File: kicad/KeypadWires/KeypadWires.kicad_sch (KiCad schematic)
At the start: 3 parts, among them J1 Cable, J2 Controller, J3 Raspberry

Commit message: Fixed keypad wiring schematics
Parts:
- removed J1: Cable, symbol Connector_Generic:Conn_02x04_Odd_Even
- added J1: Keypad, symbol Connector_Generic:Conn_02x03_Odd_Even
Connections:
- net +3.3V is gone; now on net +5V: J3.3
- net +5V: now also J1.2 (Pin_2)
- net GND: now also J1.6 (Pin_6)
- net RS232_IN: now also J1.3 (Pin_3)
- net RS232_OUT: now also J1.4 (Pin_4)
- net SCL: now also J1.5 (Pin_5)
- net SDA: now also J1.1 (Pin_1)
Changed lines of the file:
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@@
 	(wire
 		(pts
-			(xy 182.88 90.17) (xy 182.88 86.36)
+			(xy 182.88 92.71) (xy 179.07 92.71)
 		)
 		(stroke
@@
 	(wire
 		(pts
-			(xy 189.23 92.71) (xy 189.23 86.36)
-		)
-		(stroke
-			(width 0)
-			(type default)
-		)
-	)
-	(wire
-		(pts
 			(xy 180.34 97.79) (xy 180.34 99.06)
 		)
@@
 	(wire
 		(pts
-			(xy 179.07 90.17) (xy 182.88 90.17)
-		)
-		(stroke
-			(width 0)
-			(type default)
-		)
-	)
-	(wire
-		(pts
 			(xy 93.98 121.92) (xy 104.14 121.92)
 		)
@@
 	(wire
 		(pts
-			(xy 179.07 92.71) (xy 189.23 92.71)
-		)
-		(stroke
-			(width 0)
-			(type default)
-		)
-	)
-	(wire
-		(pts
 			(xy 93.98 125.73) (xy 93.98 121.92)
+		)
+		(stroke
+			(width 0)
+			(type default)
+		)
+	)
+	(wire
+		(pts
+			(xy 182.88 86.36) (xy 182.88 92.71)
 		)
 		(stroke
@@
 	)
 	(symbol
+		(lib_id "power:+5V")
+		(at 127 116.84 0)
+		(unit 1)
+		(exclude_from_sim no)
+		(in_bom yes)
+		(on_board yes)
+		(dnp no)
+		(fields_autoplaced yes)
+		(property "Reference" "#PWR01"
+			(at 127 120.65 0)
+			(effects
+				(font
+					(size 1.27 1.27)
+				)
+				(hide yes)
+			)
+		)
+		(property "Value" "+5V"
+			(at 127 111.76 0)
+			(effects
+				(font
+					(size 1.27 1.27)
+				)
+			)
+		)
+		(property "Footprint" ""
+			(at 127 116.84 0)
+			(effects
+				(font
+					(size 1.27 1.27)
+				)
+				(hide yes)
+			)
+		)
+		(property "Datasheet" ""
+			(at 127 116.84 0)
+			(effects
+				(font
+					(size 1.27 1.27)
+				)
+				(hide yes)
+			)
+		)
+		(property "Description" "Power symbol creates a global label with name \"+5V\""
+			(at 127 116.84 0)
+			(effects
+				(font
+					(size 1.27 1.27)
+				)
+				(hide yes)
+			)
+		)
+		(pin "1"
+		)
+		(instances
+			(project "KeypadWires"
+				(path "/a35776e5-918f-4787-bc96-ea4223b78852"
+					(reference "#PWR01")
+					(unit 1)
+				)
+			)
+		)
+	)
+	(symbol
 		(lib_id "power:GND")
 		(at 93.98 97.79 0)
@@
 	)
 	(symbol
-		(lib_id "Connector_Generic:Conn_02x04_Odd_Even")
-		(at 171.45 92.71 0)
-		(unit 1)
-		(exclude_from_sim no)
-		(in_bom yes)
-		(on_board yes)
-		(dnp no)
-		(fields_autoplaced yes)
-		(property "Reference" "J1"
-			(at 172.72 83.82 0)
-			(effects
-				(font
-					(size 1.27 1.27)
-				)
-			)
-		)
-		(property "Value" "Cable"
-			(at 172.72 86.36 0)
-			(effects
-				(font
-					(size 1.27 1.27)
-				)
-			)
-		)
-		(property "Footprint" ""
-			(at 171.45 92.71 0)
-			(effects
-				(font
-					(size 1.27 1.27)
-				)
-				(hide yes)
-			)
-		)
-		(property "Datasheet" "~"
-			(at 171.45 92.71 0)
-			(effects
-				(font
-					(size 1.27 1.27)
-				)
-				(hide yes)
-			)
-		)
-		(property "Description" "Generic connector, double row, 02x04, odd/even pin numbering scheme (row 1 odd numbers, row 2 even numbers), script generated (kicad-library-utils/schlib/autogen/connector/)"
-			(at 171.45 92.71 0)
-			(effects
-				(font
-					(size 1.27 1.27)
-				)
-				(hide yes)
-			)
-		)
-		(pin "8"
-		)
-		(pin "3"
-		)
-		(pin "2"
-		)
-		(pin "7"
-		)
-		(pin "6"
-		)
-		(pin "5"
-		)
-		(pin "1"
-		)
-		(pin "4"
-		)
-		(instances
-			(project "KeypadWires"
-				(path "/a35776e5-918f-4787-bc96-ea4223b78852"
-					(reference "J1")
-					(unit 1)
-				)
-			)
-		)
-	)
-	(symbol
 		(lib_id "power:+5V")
 		(at 138.43 92.71 0)
@@
 	)
 	(symbol
-		(lib_id "power:+3.3V")
-		(at 127 116.84 0)
+		(lib_id "Connector_Generic:Conn_02x03_Odd_Even")
+		(at 171.45 95.25 0)
 		(unit 1)
 		(exclude_from_sim no)
@@
 		(dnp no)
 		(fields_autoplaced yes)
-		(property "Reference" "#PWR08"
-			(at 127 120.65 0)
-			(effects
-				(font
-					(size 1.27 1.27)
-				)
-				(hide yes)
-			)
-		)
-		(property "Value" "+3.3V"
-			(at 127 111.76 0)
+		(property "Reference" "J1"
+			(at 172.72 86.36 0)
+			(effects
+				(font
+					(size 1.27 1.27)
+				)
+			)
+		)
+		(property "Value" "Keypad"
+			(at 172.72 88.9 0)
 			(effects
 				(font
@@
 		)
 		(property "Footprint" ""
-			(at 127 116.84 0)
-			(effects
-				(font
-					(size 1.27 1.27)
-				)
-				(hide yes)
-			)
-		)
-		(property "Datasheet" ""
-			(at 127 116.84 0)
-			(effects
-				(font
-					(size 1.27 1.27)
-				)
-				(hide yes)
-			)
-		)
-		(property "Description" "Power symbol creates a global label with name \"+3.3V\""
-			(at 127 116.84 0)
-			(effects
-				(font
-					(size 1.27 1.27)
-				)
-				(hide yes)
-			)
+			(at 171.45 95.25 0)
+			(effects
+				(font
+					(size 1.27 1.27)
+				)
+				(hide yes)
+			)
+		)
+		(property "Datasheet" "~"
+			(at 171.45 95.25 0)
+			(effects
+				(font
+					(size 1.27 1.27)
+				)
+				(hide yes)
+			)
+		)
+		(property "Description" "Generic connector, double row, 02x03, odd/even pin numbering scheme (row 1 odd numbers, row 2 even numbers), script generated (kicad-library-utils/schlib/autogen/connector/)"
+			(at 171.45 95.25 0)
+			(effects
+				(font
+					(size 1.27 1.27)
+				)
+				(hide yes)
+			)
+		)
+		(pin "3"
+		)
+		(pin "2"
 		)
 		(pin "1"
+		)
+		(pin "4"
+		)
+		(pin "5"
+		)
+		(pin "6"
 		)
 		(instances
 			(project "KeypadWires"
 				(path "/a35776e5-918f-4787-bc96-ea4223b78852"
-					(reference "#PWR08")
+					(reference "J1")
 					(unit 1)
 				)
-			)
-		)
-	)
-	(symbol
-		(lib_id "power:+3.3V")
-		(at 189.23 86.36 0)
-		(unit 1)
-		(exclude_from_sim no)
-		(in_bom yes)
-		(on_board yes)
-		(dnp no)
-		(fields_autoplaced yes)
-		(property "Reference" "#PWR07"
-			(at 189.23 90.17 0)
-			(effects
-				(font
-					(size 1.27 1.27)
-				)
-				(hide yes)
-			)
-		)
-		(property "Value" "+3.3V"
-			(at 189.23 81.28 0)
-			(effects
-				(font
-					(size 1.27 1.27)
-				)
-			)
-		)
-		(property "Footprint" ""
-			(at 189.23 86.36 0)
-			(effects
-				(font
-					(size 1.27 1.27)
-				)
-				(hide yes)
-			)
-		)
-		(property "Datasheet" ""
-			(at 189.23 86.36 0)
-			(effects
-				(font
-					(size 1.27 1.27)
-				)
-				(hide yes)
-			)
-		)
-		(property "Description" "Power symbol creates a global label with name \"+3.3V\""
-			(at 189.23 86.36 0)
-			(effects
-				(font
-					(size 1.27 1.27)
-				)
-				(hide yes)
-			)
-		)
-		(pin "1"
-		)
-		(instances
-			(project "KeypadWires"
-				(path "/a35776e5-918f-4787-bc96-ea4223b78852"
-					(reference "#PWR07")
-					(unit 1)
-				)

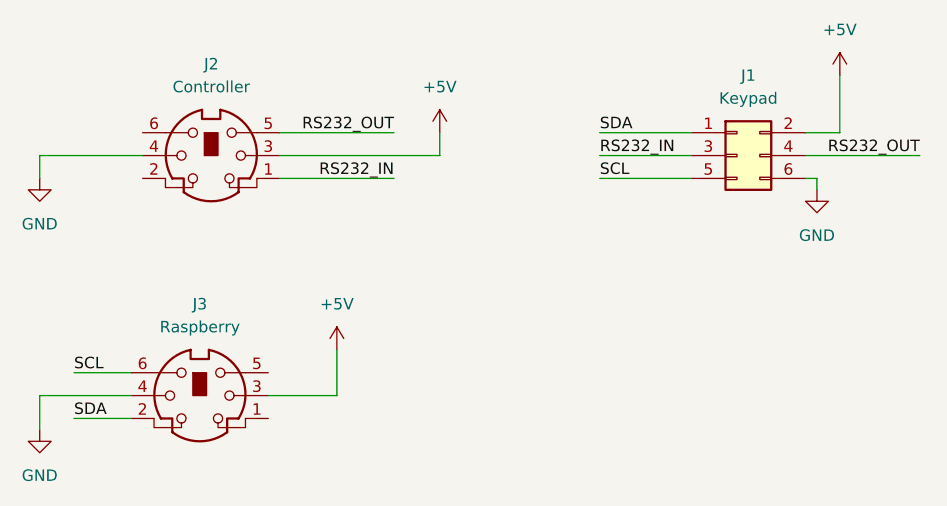
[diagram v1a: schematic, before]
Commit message: Complete schematics, using UART for communications
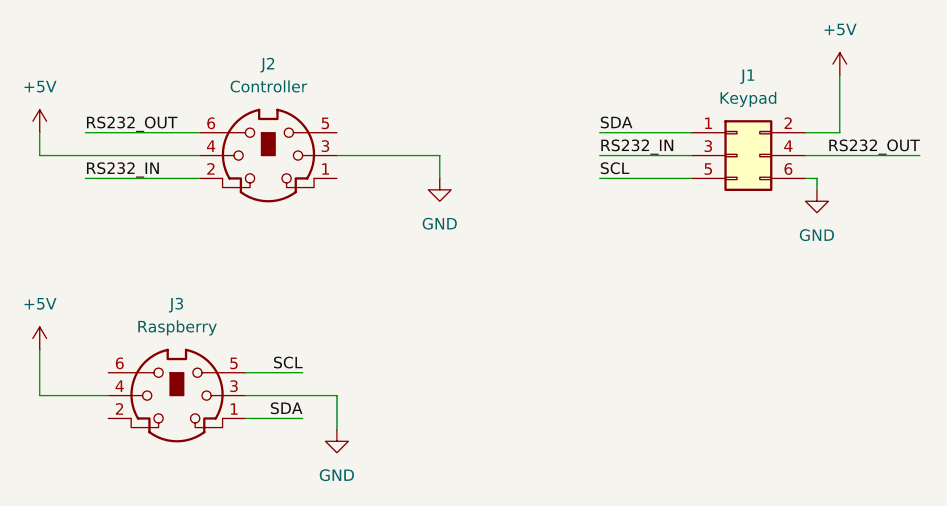
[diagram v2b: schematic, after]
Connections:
- net +5V: now also J2.4, J3.4; no longer J2.3, J3.3
- net GND: now also J2.3, J3.3; no longer J2.4, J3.4
- net RS232_IN: now also J2.2; no longer J2.1
- net RS232_OUT: now also J2.6; no longer J2.5
- net SCL: now also J3.5; no longer J3.6
- net SDA: now also J3.1; no longer J3.2
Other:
- moved on the sheet: J2, J3
